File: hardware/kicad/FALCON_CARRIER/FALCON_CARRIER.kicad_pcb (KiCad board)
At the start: 2 copper layers, 200 x 160 mm, 55 parts, among them J1 B2P-VH-FB-B, J10 BM03B-GHS-TBT, J11 470531000, J12 BM04B-GHS-TBT, J13 470531000, J2 BM04B-GHS-TBT, J3 GPS_UART, J4 INA260_BAT_LOGIC, J5 INA260_SOLAR_0X41, J6 BM04B-GHS-TBT, J7 BM03B-GHS-TBT, J8 BM03B-GHS-TBT, J9 BM03B-GHS-TBT, Q1 2N7002_FAN1_PWM, Q2 2N7002_FAN2_PWM, U1 AP2112K-3.3TRG1, U2 ESP32-DevKitC_V4_WROOM-32E, U3 BNO085_SPI, U4 ADS1115_0X48, U6 EFUSE_TPS25947_TBD

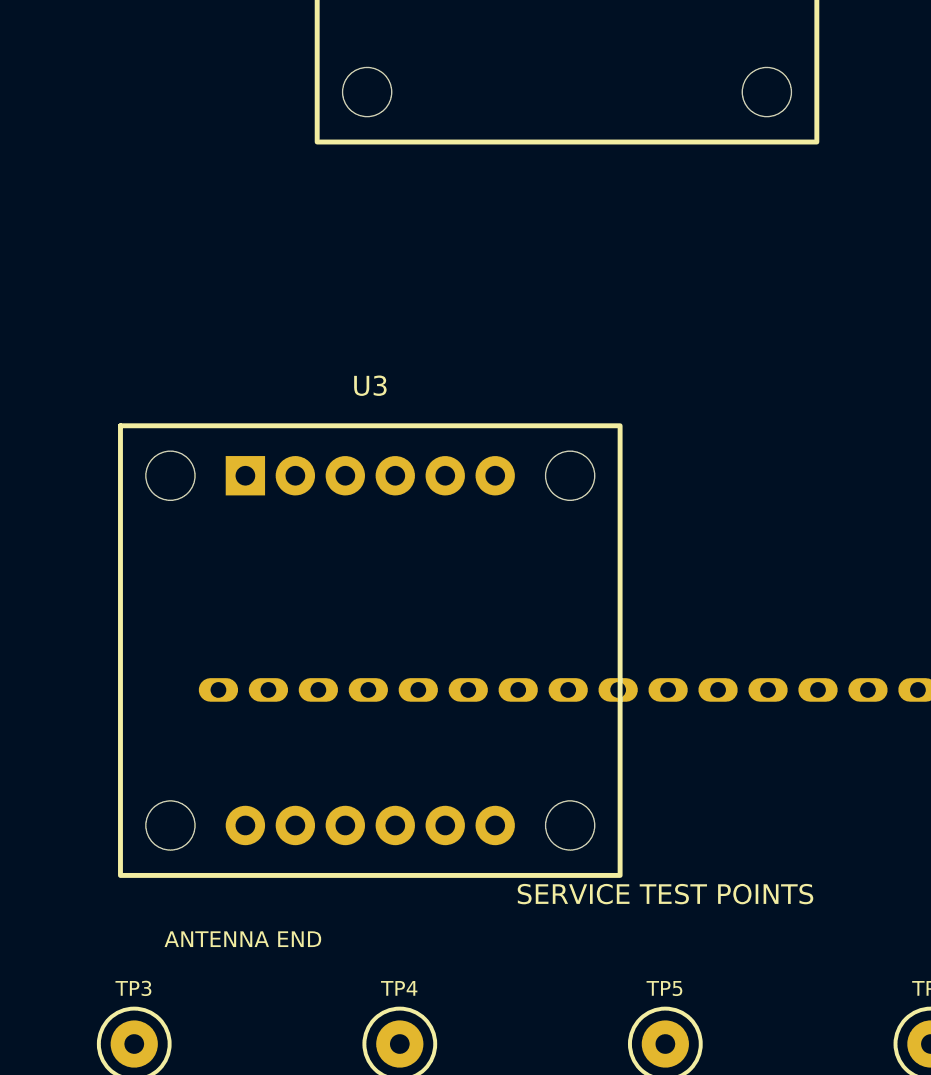
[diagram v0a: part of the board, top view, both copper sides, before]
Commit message: Add recognizable PCB sample-part models
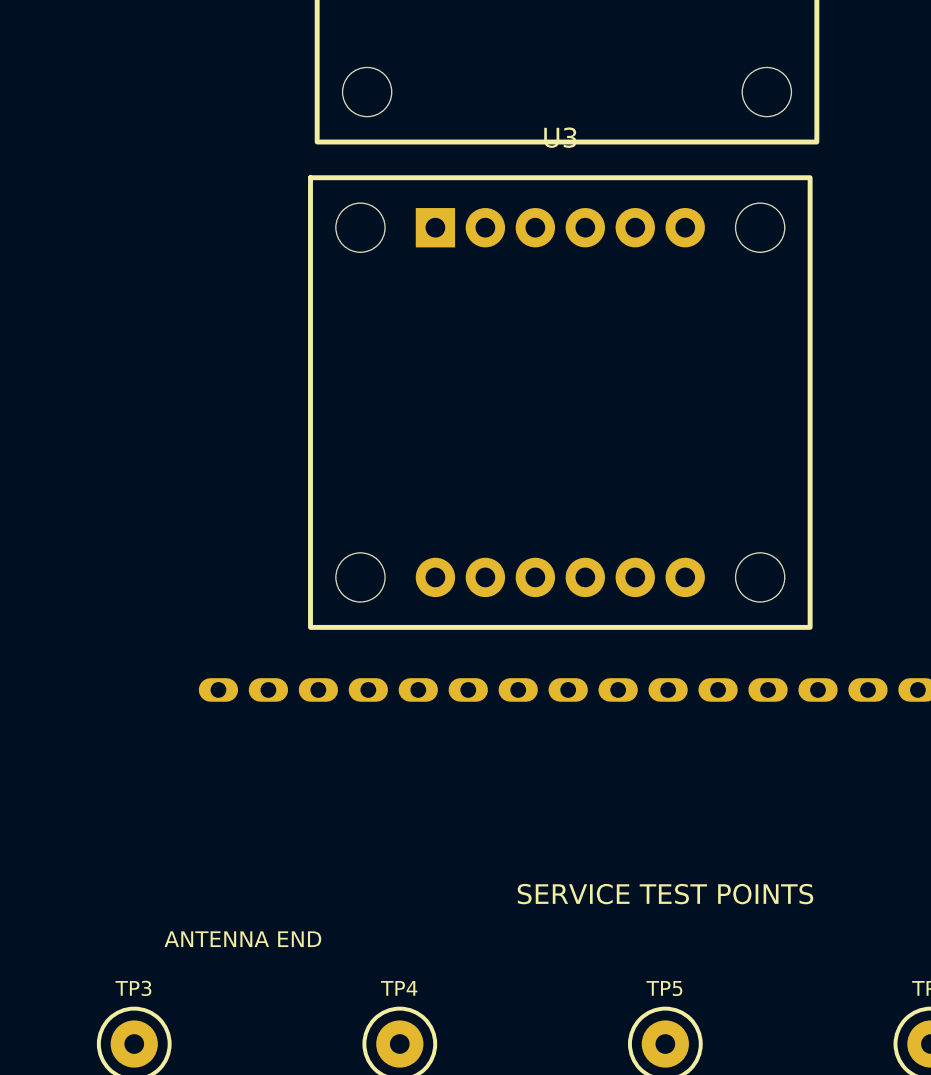
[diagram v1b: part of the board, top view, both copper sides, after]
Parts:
- moved U3 15.9 mm to (144.7, 75.4)

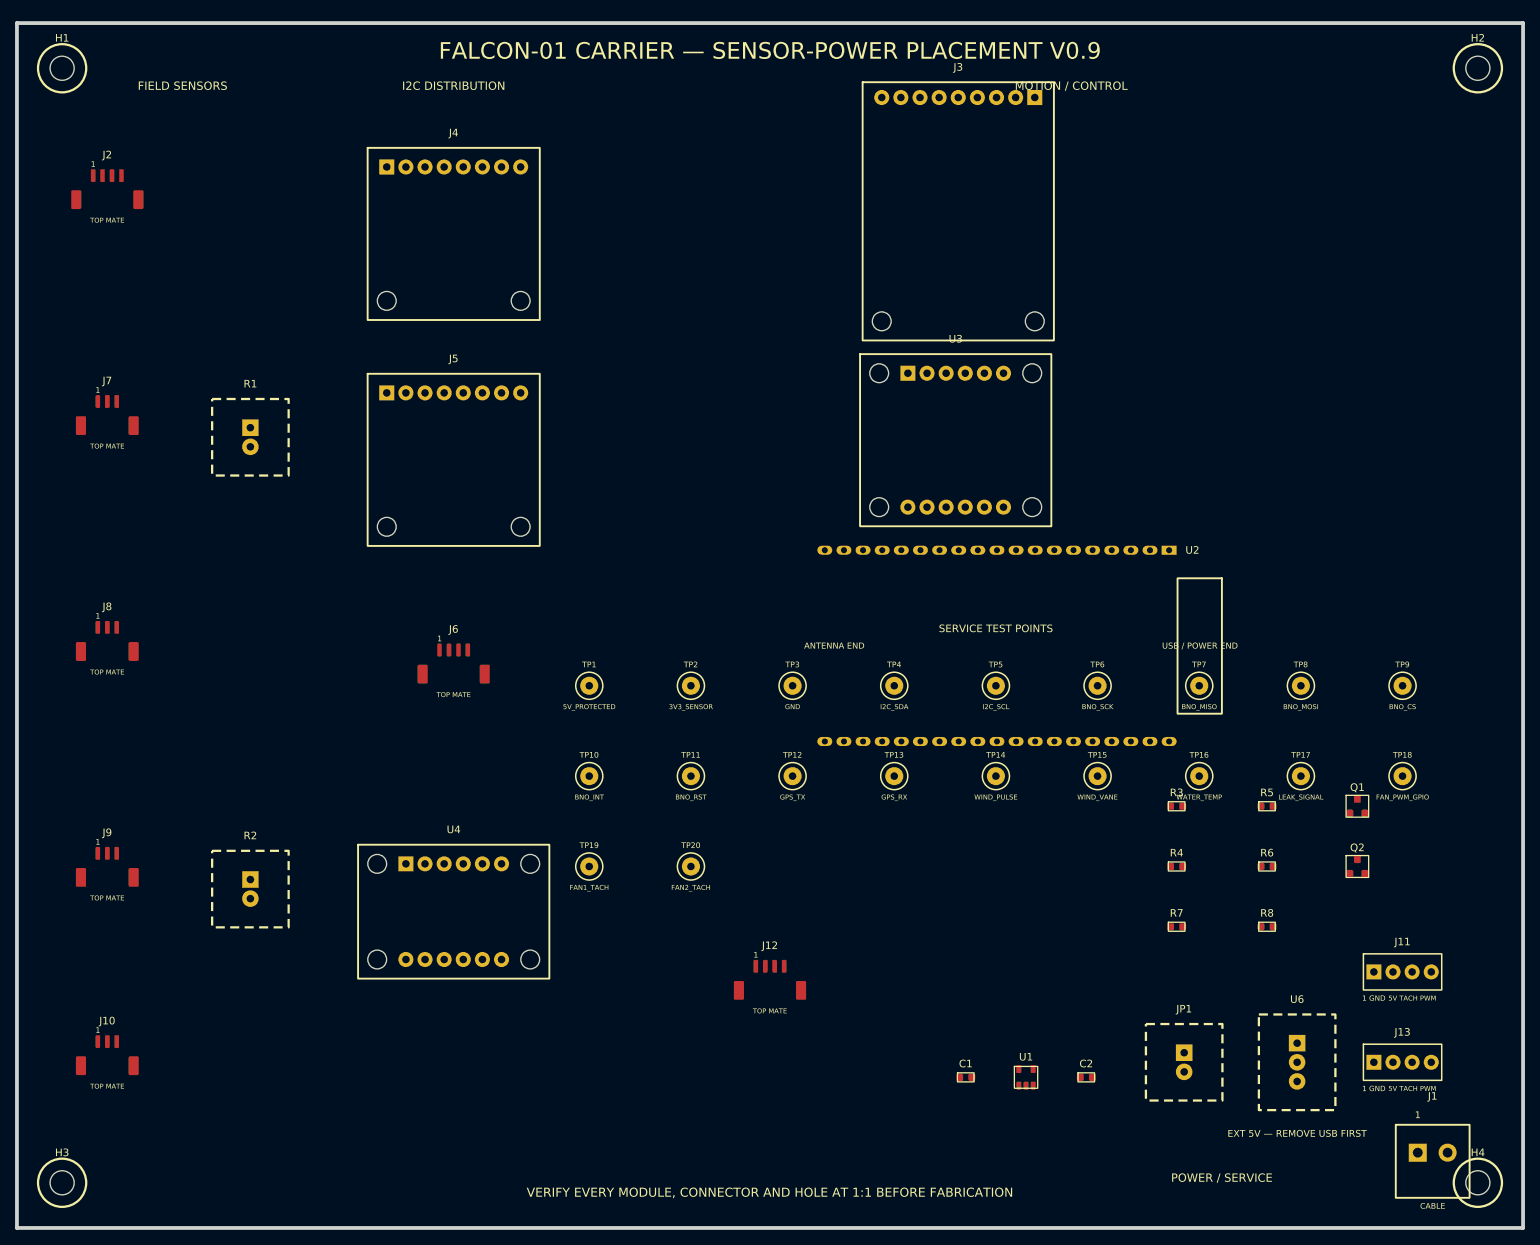
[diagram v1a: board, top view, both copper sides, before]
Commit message: Compact PCB preview placement
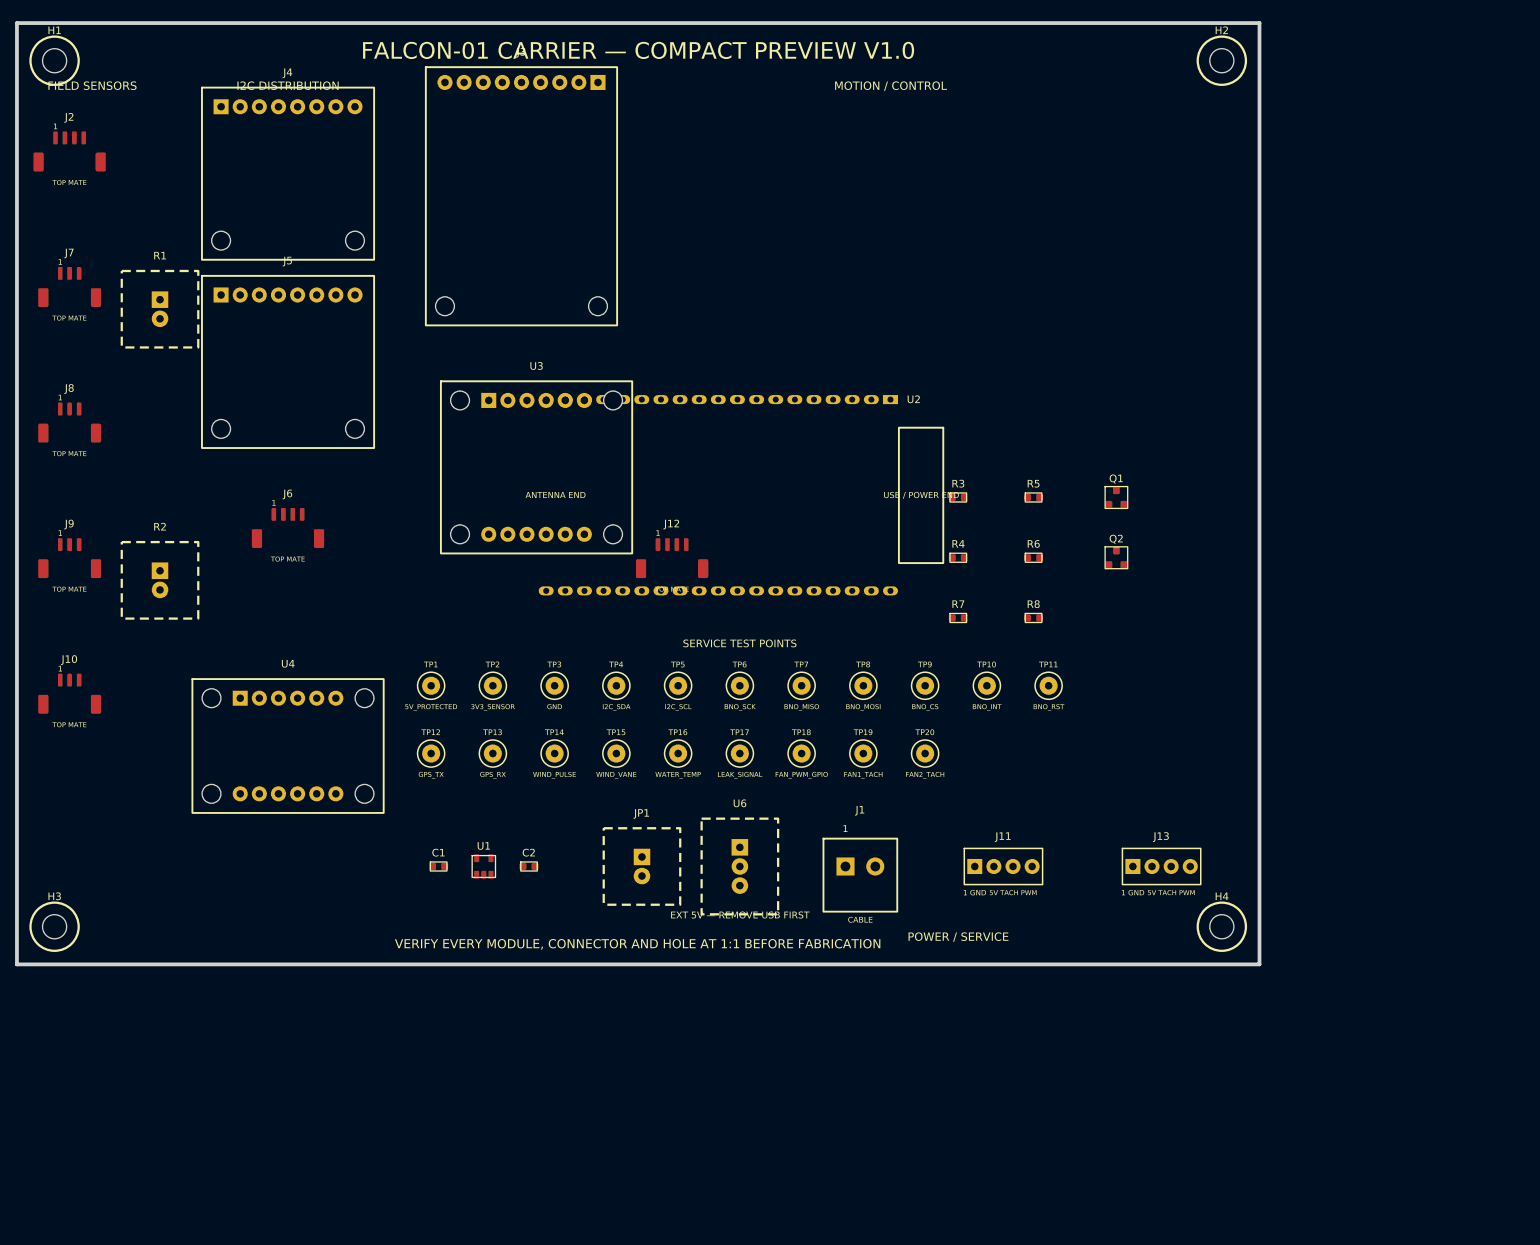
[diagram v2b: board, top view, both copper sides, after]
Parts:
- moved J1 85.0 mm to (132.0, 132.0)
- moved TP18 79.9 mm to (124.2, 117.0)
- moved C2 79.1 mm to (88.0, 132.0)
- moved U6 78.4 mm to (116.0, 132.0)
- moved U1 77.3 mm to (82.0, 132.0)
- moved JP1 76.6 mm to (103.0, 132.0)
- moved C1 75.4 mm to (76.0, 132.0)
- moved TP17 74.6 mm to (116.0, 117.0)
- moved TP16 69.3 mm to (107.8, 117.0)
- moved TP15 64.0 mm to (99.6, 117.0)
- moved TP9 63.4 mm to (140.6, 108.0)
- moved TP14 58.7 mm to (91.4, 117.0)
- moved TP8 58.1 mm to (132.4, 108.0)
- moved J3 58.0 mm to (87.0, 43.0)
- moved J12 57.5 mm to (107.0, 94.0)
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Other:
- board size 200 x 160 mm -> 165 x 125 mm
- board text added: "FALCON-01 CARRIER — COMPACT PREVIEW V1.0"
- board text removed: "FALCON-01 CARRIER — SENSOR-POWER PLACEMENT V0.9"

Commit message: Correct compact PCB component placement
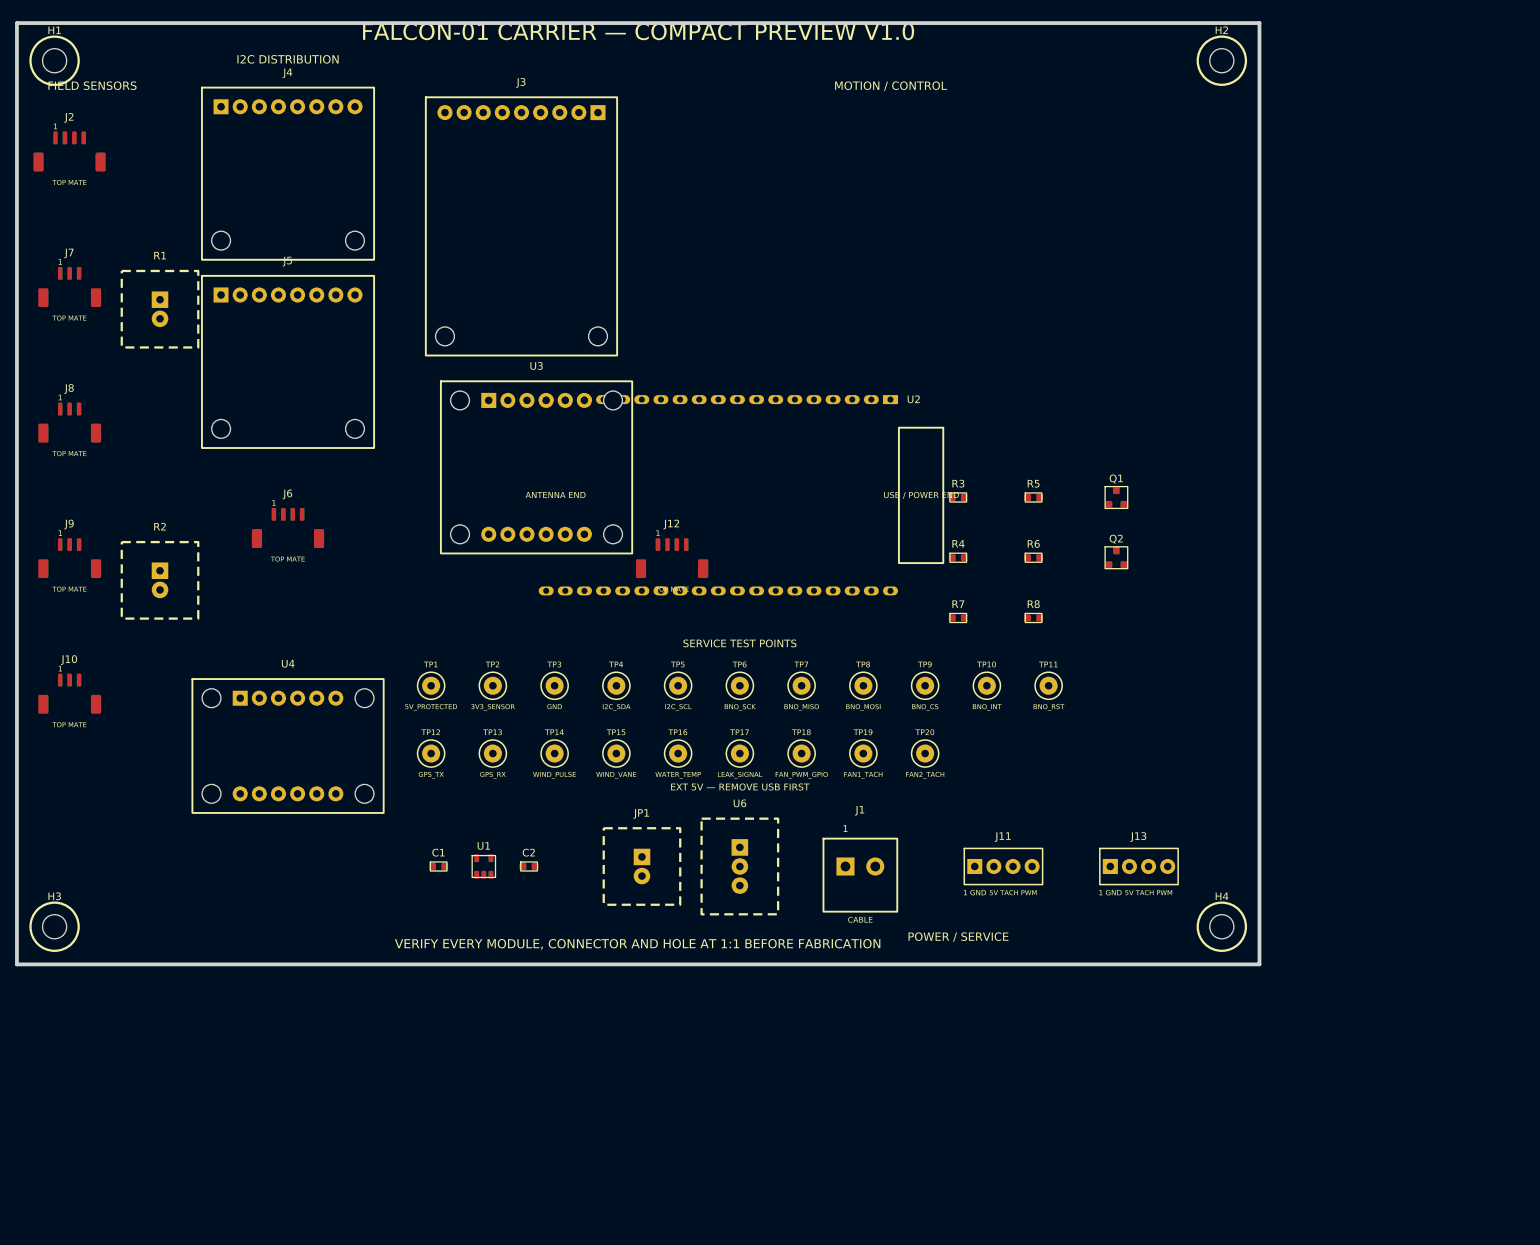
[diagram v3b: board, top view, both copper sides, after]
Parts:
- moved J3 4.00 mm to (87.0, 47.0)
- moved J13 3.00 mm to (169.0, 132.0)
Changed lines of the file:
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@@
 	(footprint "MOLEX_470531000_4PIN_FAN_HEADER"
 		(layer "F.Cu")
-		(at 172 132)
+		(at 169 132)
 		(descr "Molex 470531000 4-circuit 2.54 mm vertical fan header; outline verify on receipt")
 		(tags "MOLEX 47053 FAN PWM 2.54MM")
@@
 	(footprint "FALCON_LOCKED_GPS_UART"
 		(layer "F.Cu")
-		(at 87 43)
+		(at 87 47)
 		(descr "Adafruit Ultimate GPS PID 746 official Eagle CAD; receiving check still required")
 		(tags "FALCON MANUFACTURER CAD SOCKET")
@@
 	)
 	(gr_text "EXT 5V — REMOVE USB FIRST"
-		(at 116 139 0)
+		(at 116 122 0)
 		(layer "F.SilkS")
 		(effects
@@
 	)
 	(gr_text "I2C DISTRIBUTION"
-		(at 56 29 0)
+		(at 56 25.5 0)
 		(layer "F.SilkS")
 		(effects
@@
 	)
 	(gr_text "FALCON-01 CARRIER — COMPACT PREVIEW V1.0"
-		(at 102.5 25 0)
+		(at 102.5 22.5 0)
 		(layer "F.SilkS")
 		(effects
